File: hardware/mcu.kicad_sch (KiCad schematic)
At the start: 56 parts, among them J10 PRPC004SAAN-RC, J7 PRPC006SAAN-RC, J8 PRPC001DAAN-RC, J9 PRPC006SAAN-RC, U3 AT25SF081B-SSHD-B, U4 MCP9808, U5 STM32L552CEU6, Y1 ECS-160-9-37-CKM-TR3, Y2 ABS05-32.768KHZ-9-T

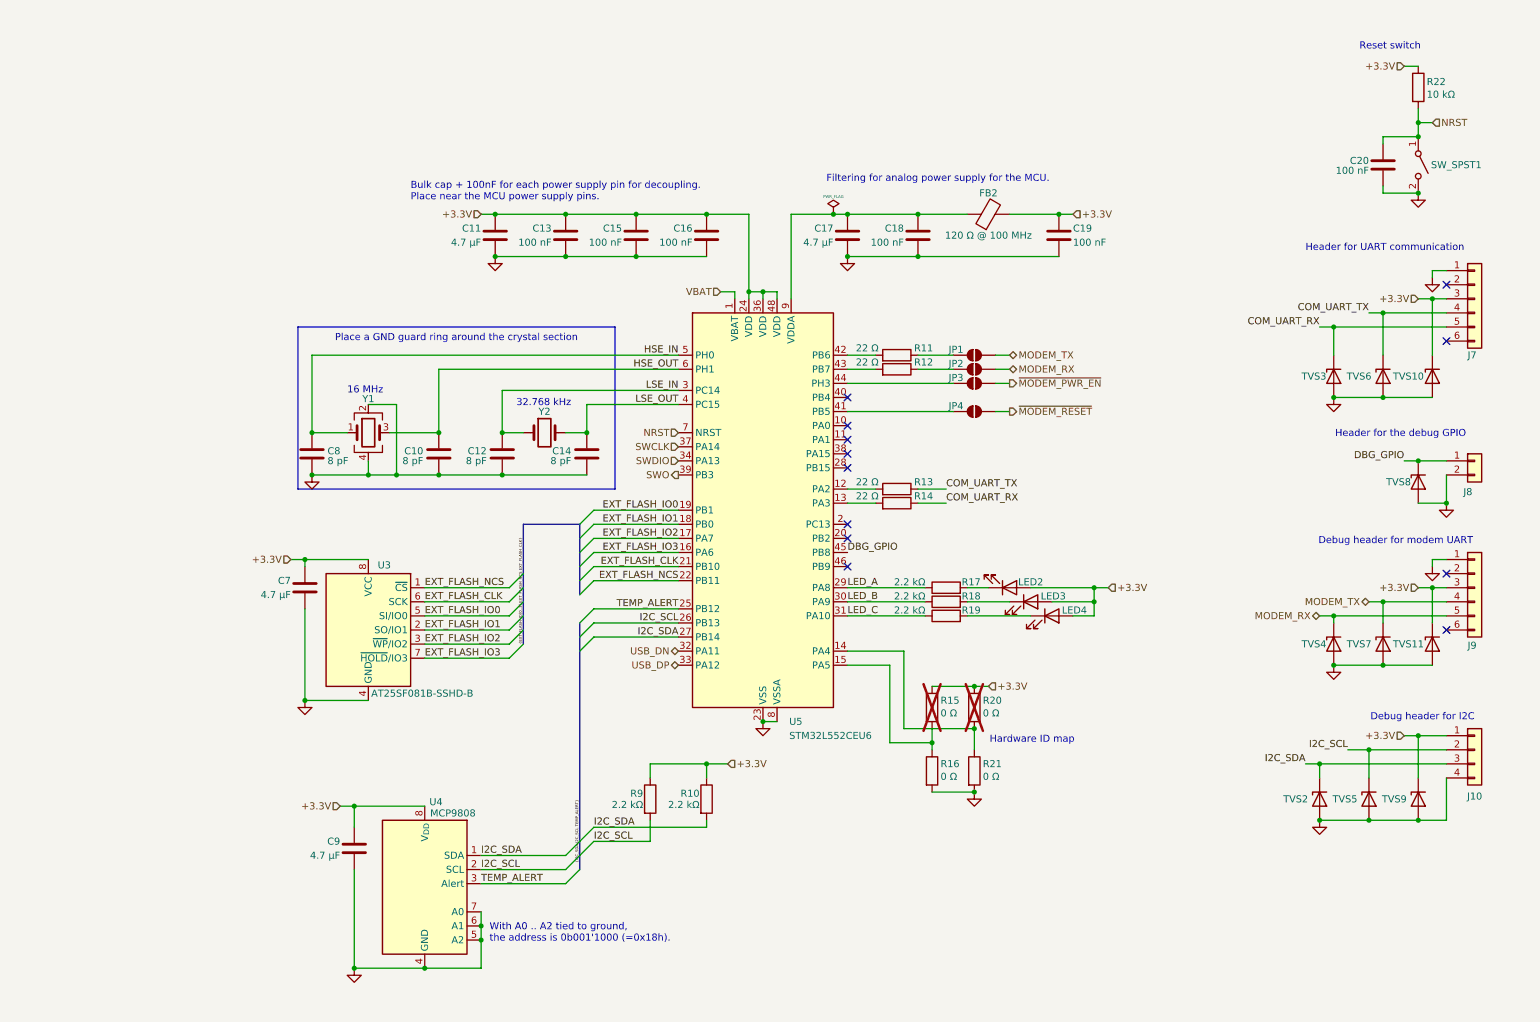
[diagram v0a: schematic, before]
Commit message: HW: Start adding Li-Po support
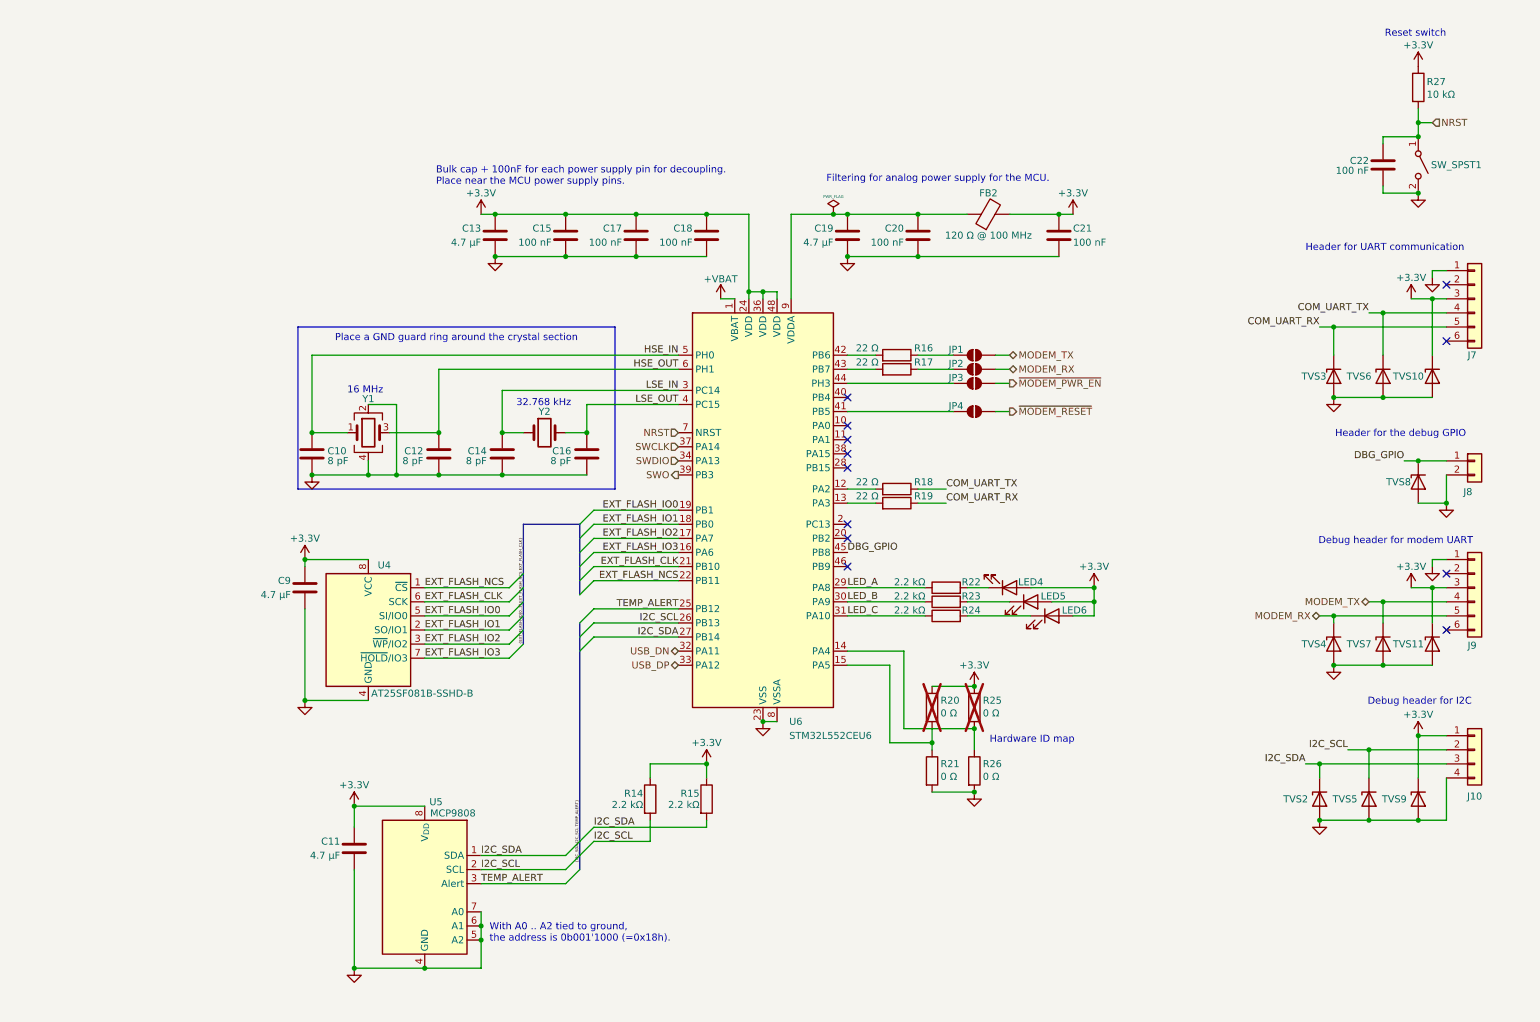
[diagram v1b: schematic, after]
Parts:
- renumbered C8 to C10, C9 to C11, C10 to C12, C11 to C13, C12 to C14, C13 to C15, C14 to C16, C15 to C17, C16 to C18, C17 to C19, C18 to C20, C19 to C21, C20 to C22, C7 to C9, LED2 to LED4, LED3 to LED5, LED4 to LED6, R9 to R14, R10 to R15, R11 to R16, R12 to R17, R13 to R18, R14 to R19, R15 to R20, R16 to R21, R17 to R22, R18 to R23, R19 to R24, R20 to R25, R21 to R26, R22 to R27, U3 to U4, U4 to U5, U5 to U6
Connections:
- net VBAT renamed +VBAT

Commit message: HW: Replace STM QFN with QFP
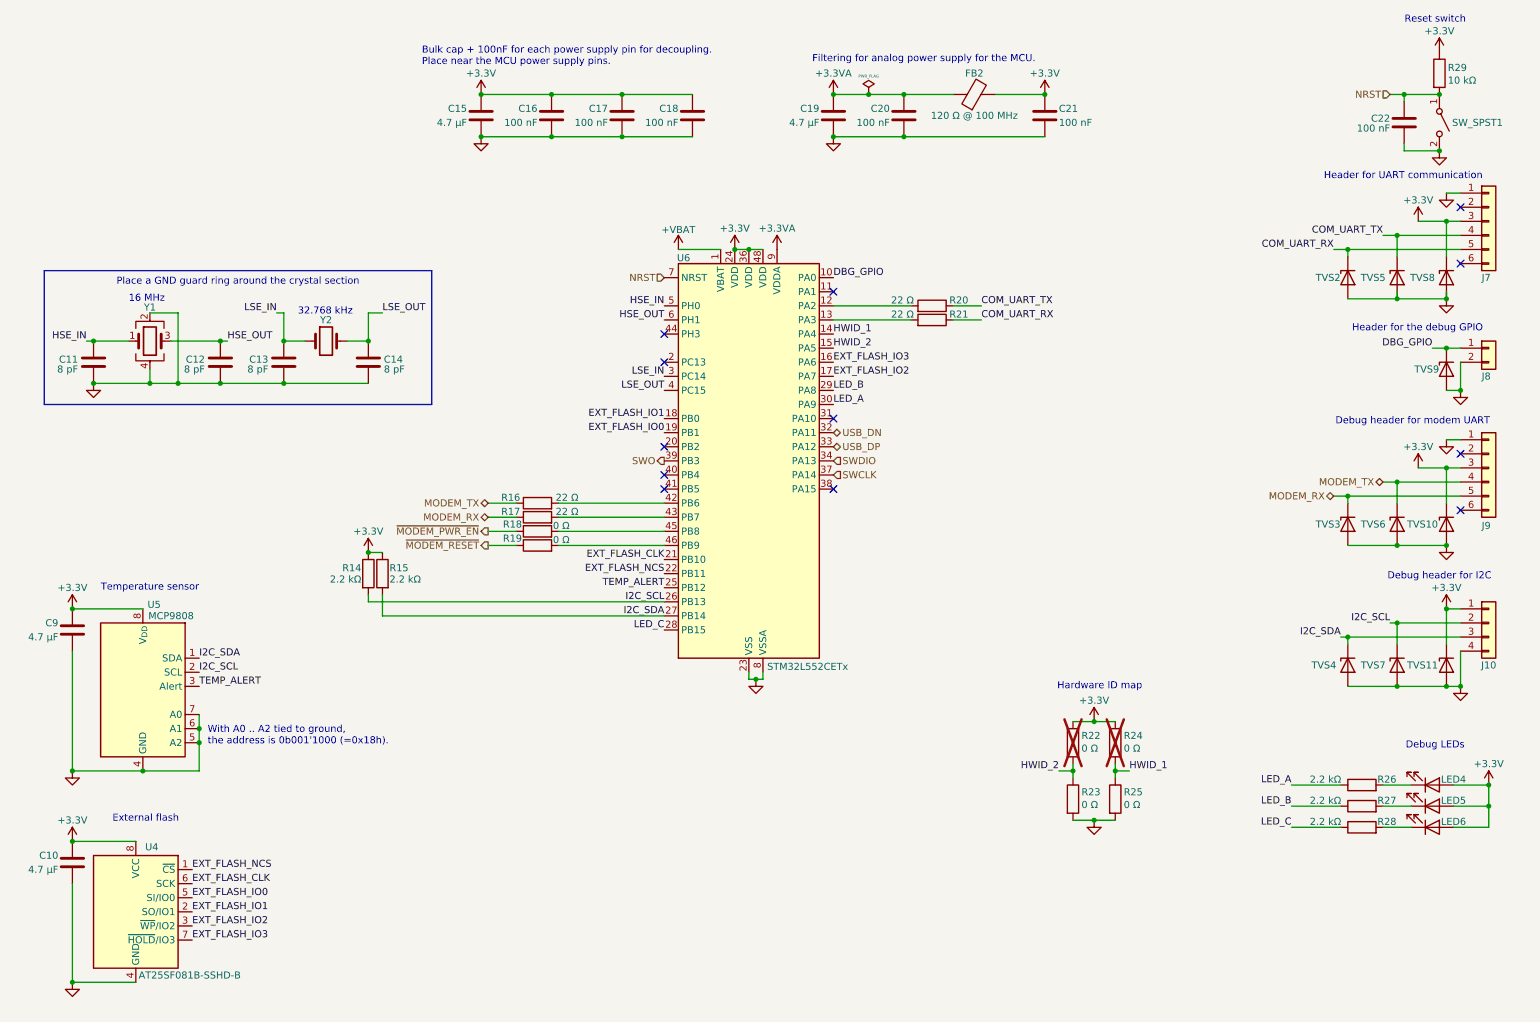
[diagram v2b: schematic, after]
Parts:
- removed JP1, JP2, JP3, JP4: SolderJumper_2_Open, Jumper:SolderJumper-2_P1.3mm_Open_RoundedPad1.0x1.5mm, symbol Jumper:SolderJumper_2_Open
- removed U6: STM32L552CEU6, Package_DFN_QFN:QFN-48-1EP_7x7mm_P0.5mm_EP5.6x5.6mm, symbol STM32L552CEU6:STM32L552CEUx
- added R18, R19: 0 Ω, perfect_footprints:0402_1005_perfect, symbol Device:R
- added U6: STM32L552CETx, Package_DFN_QFN:QFN-48-1EP_7x7mm_P0.5mm_EP3.5x3.5mm, symbol MCU_ST_STM32L5:STM32L552CETx
- renumbered C9 to C10, C10 to C11, C14 to C13, C16 to C14, C13 to C15, C15 to C16, C11 to C9, R15 to R14, R14 to R15, R18 to R20, R19 to R21, R20 to R22, R21 to R23, R25 to R24, R26 to R25, R22 to R26, R23 to R27, R24 to R28, R27 to R29, TVS11 to TVS10, TVS9 to TVS11, TVS3 to TVS2, TVS4 to TVS3, TVS2 to TVS4, TVS6 to TVS5, TVS7 to TVS6, TVS5 to TVS7, TVS10 to TVS8, TVS8 to TVS9
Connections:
- net +3.3V: now also U6.24 (VDD), U6.36 (VDD), U6.48 (VDD)
- net +VBAT: now also U6.1 (VBAT)
- net DBG_GPIO: now also U6.10 (PA0)
- net EXT_FLASH_CLK: now also U6.21 (PB10)
- net EXT_FLASH_IO0: now also U6.19 (PB1)
- net EXT_FLASH_IO1: now also U6.18 (PB0)
- net EXT_FLASH_IO2: now also U6.17 (PA7)
- net EXT_FLASH_IO3: now also U6.16 (PA6)
- net EXT_FLASH_NCS: now also U6.22 (PB11)
- net GND: now also U6.23 (VSS), U6.35 (VSS), U6.47 (VSS), U6.8 (VSSA)
- net HSE_IN: now also U6.5 (PH0)
- net HSE_OUT: now also U6.6 (PH1)
- net I2C_SCL: now also R14.2, U6.26 (PB13); no longer R15.2
- net I2C_SDA: now also R15.2, U6.27 (PB14); no longer R14.2
- net LED_A: now also U6.30 (PA9)
- net LED_B: now also U6.29 (PA8)
- net LED_C: now also U6.28 (PB15)
- net LSE_IN: now also U6.3 (PC14)
- net LSE_OUT: now also U6.4 (PC15)
- net MODEM_RX: now also R17.1
- net MODEM_TX: now also R16.1
- net NRST: now also U6.7 (NRST)
- net SWCLK: now also U6.37 (PA14)
- net SWDIO: now also U6.34 (PA13)
- net SWO: now also U6.39 (PB3)
- net TEMP_ALERT: now also U6.25 (PB12)
- net USB_DN: now also U6.32 (PA11)
- net USB_DP: now also U6.33 (PA12)
- net ~{MODEM_PWR_EN}: now also R18.1
- net ~{MODEM_RESET}: now also R19.1
- net HWID_2: now reaches R22.2, R23.1
- net HWID_2: now also U6.15 (PA5)
- net +3.3VA: now reaches C19.1, C20.1, FB2.1
- net +3.3VA: now also U6.9 (VDDA)
- net at R17.2: now also U6.43 (PB7)
- net at R20.2: now also U6.12 (PA2)
- net at R16.2: now also U6.42 (PB6)
- net at R21.2: now also U6.13 (PA3)
- net HWID_1: now reaches R24.2, R25.1
- net HWID_1: now also U6.14 (PA4)
- new net: R18.2, U6.45 (PB8)
- new net: R19.2, U6.46 (PB9)
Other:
- note added: "Debug LEDs"
- note added: "External flash"
- note added: "Temperature sensor"
- moved on the sheet: C10, C11, C12, C13, C14, C15, C16, C17, C18, C19, C20, C21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

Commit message: HW: Replace TC2050 wiht 10-pin connector
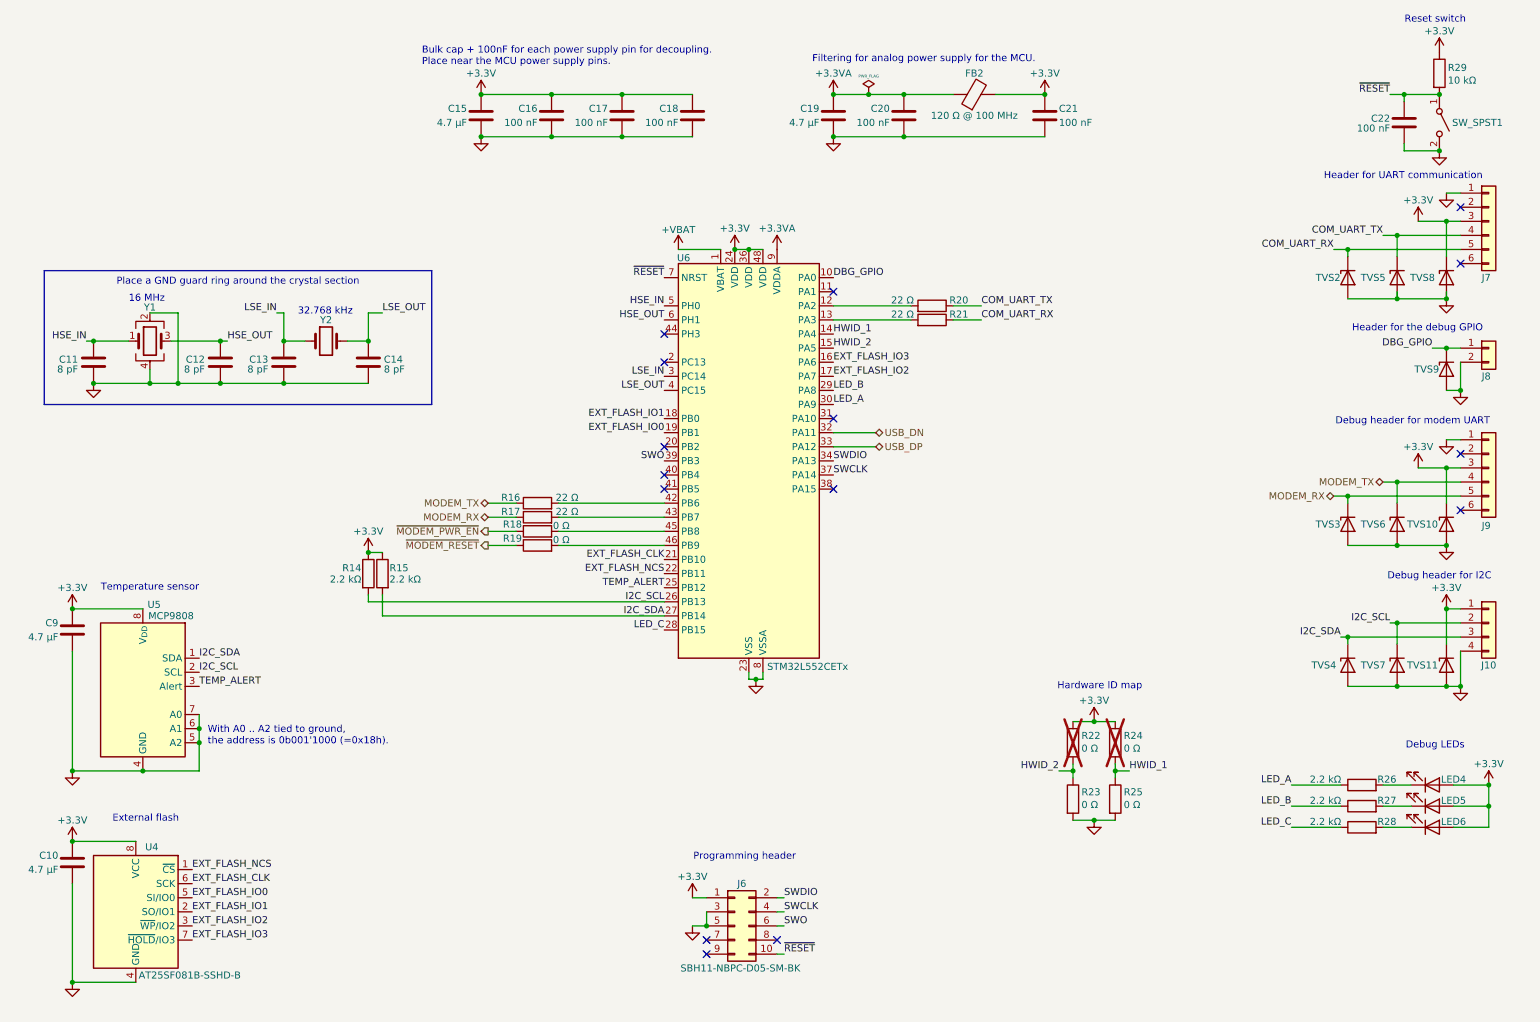
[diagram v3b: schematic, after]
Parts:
- added J6: SBH11-NBPC-D05-SM-BK, Connector_PinHeader_2.54mm:PinHeader_2x05_P2.54mm_Vertical_SMD, symbol Connector_Generic:Conn_02x05_Odd_Even
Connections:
- net +3.3V: now also J6.1 (Pin_1)
- net GND: now also J6.3 (Pin_3), J6.5 (Pin_5)
- net SWCLK: now also J6.4 (Pin_4)
- net SWDIO: now also J6.2 (Pin_2)
- net SWO: now also J6.6 (Pin_6)
- net NRST renamed ~{RESET}
- net ~{RESET}: now also J6.10 (Pin_10)
- no-connect marks 12 -> 15
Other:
- note added: "Programming header"
